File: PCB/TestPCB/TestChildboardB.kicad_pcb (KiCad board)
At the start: 2 copper layers, 61.2 x 100.1 mm, 5 parts, among them M2 Screw MountingHole_2.2mm_M2

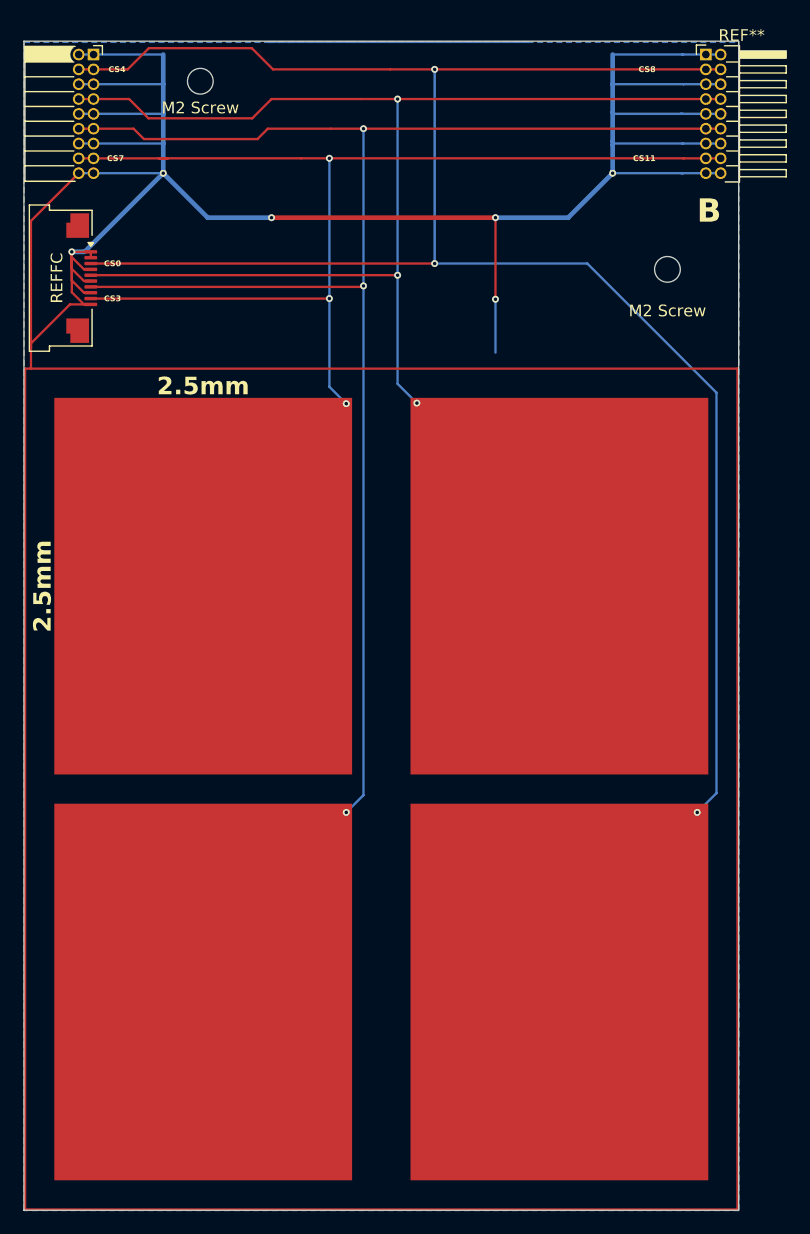
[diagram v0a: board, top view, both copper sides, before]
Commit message: Modify test pcb, add flow chart
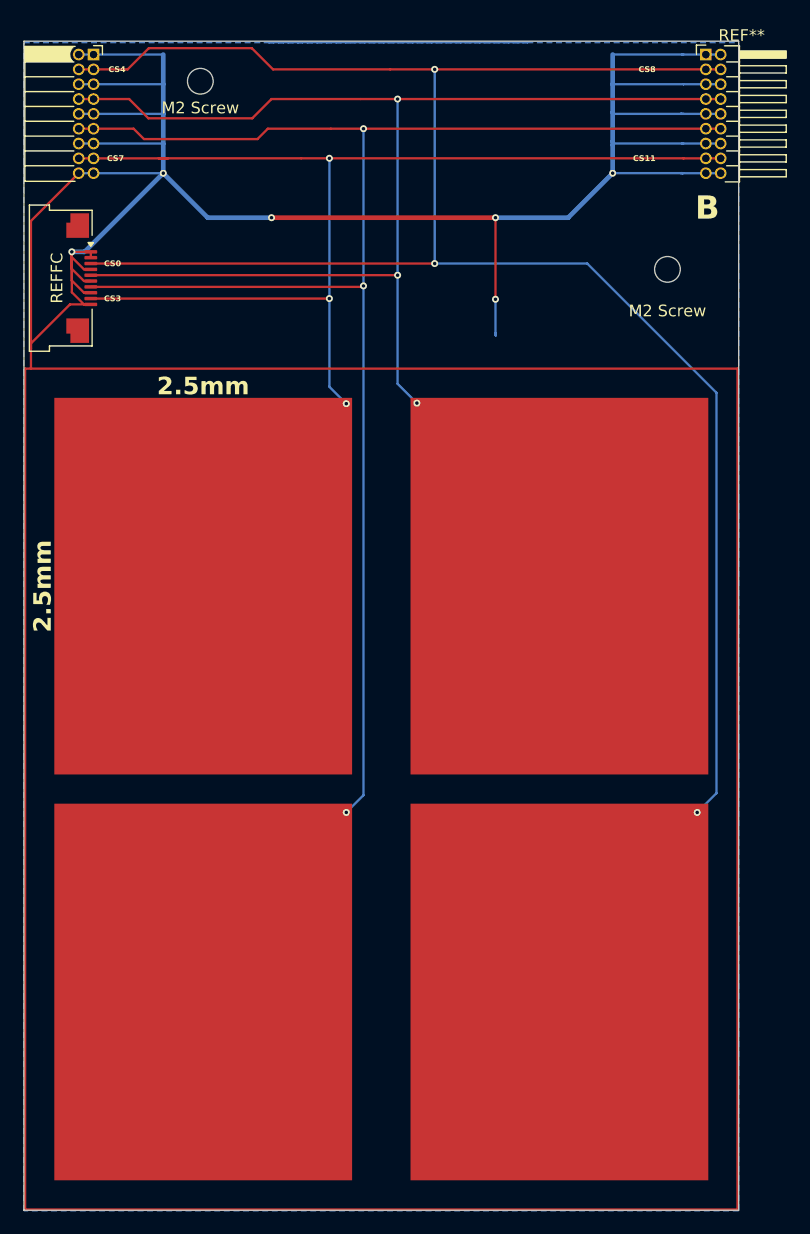
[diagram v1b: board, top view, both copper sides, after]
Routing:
- net GND: track 211.1 -> 209.9 mm
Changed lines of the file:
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@@
 		(capping no)
 		(filling no)
+		(zone_defaults)
 		(pcbplotparams
 			(layerselection 0x00000000_00000000_55555555_5755f5ff)
@@
 		)
 	)
-	(gr_text "B\n"
-		(at 74.5236 29.1592 0)
+	(gr_text "B"
+		(at 74.3712 28.9052 0)
 		(layer "F.SilkS" knockout)
 		(effects
@@
 	)
 	(segment
+		(start 57.277 38.6334)
+		(end 57.3024 38.6588)
+		(width 0.2)
+		(layer "B.Cu")
+		(net "GND")
+	)
+	(segment
 		(start 73.284 22.225)
 		(end 73.279 22.22)
@@
 	)
 	(segment
+		(start 57.3024 38.5064)
+		(end 57.2516 38.4556)
+		(width 0.2)
+		(layer "B.Cu")
+		(net "GND")
+	)
+	(segment
 		(start 73.371 22.22)
 		(end 73.279 22.22)
@@
 	)
 	(segment
+		(start 57.277 35.56)
+		(end 57.277 38.6334)
+		(width 0.2)
+		(layer "B.Cu")
+		(net "GND")
+	)
+	(segment
 		(start 67.31 19.558)
 		(end 67.31 17.145)
@@
 	)
 	(segment
-		(start 57.277 35.56)
-		(end 57.277 40.132)
-		(width 0.2)
-		(layer "B.Cu")
-		(net "GND")
-	)
-	(segment
 		(start 67.315 24.76)
 		(end 67.31 24.765)
@@
 	)
 	(segment
+		(start 57.3024 38.6588)
+		(end 57.3024 38.5064)
+		(width 0.2)
+		(layer "B.Cu")
+		(net "GND")
+	)
+	(segment
 		(start 28.829 24.765)
 		(end 32.639 28.575)
@@
 		(polygon
 			(pts
-				(xy 16.9164 13.5636) (xy 60.088771 13.5636) (xy 44.958 13.5636) (xy 37.82973 13.566309) (xy 78.136607 13.565179)
-				(xy 78.126782 113.5888) (xy 16.9164 113.5888)
+				(xy 16.888606 13.587381) (xy 60.060977 13.587381) (xy 44.930206 13.587381) (xy 37.801936 13.59009)
+				(xy 78.108813 13.58896) (xy 78.098988 113.612581) (xy 16.888606 113.612581)
 			)
 		)
